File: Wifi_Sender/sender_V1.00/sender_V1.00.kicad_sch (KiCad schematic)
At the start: 2 parts, among them U1 ESP32-DevKitC, U2 L298N

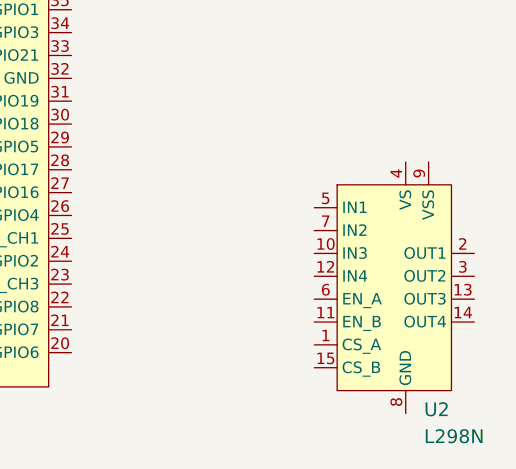
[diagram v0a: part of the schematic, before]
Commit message: Removed old Pics
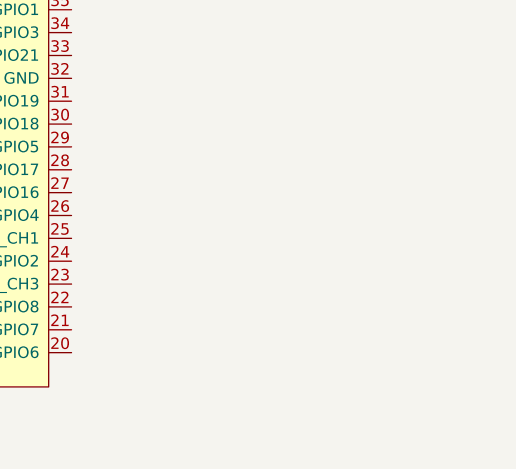
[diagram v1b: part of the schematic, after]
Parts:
- removed U2: L298N, digikey-footprints:Multiwatt-15, symbol dk_PMIC-Full-Half-Bridge-Drivers:L298N
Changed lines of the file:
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@@
-    (pin "9")
-  )
-  (symbol (lib_id "dk_PMIC-Full-Half-Bridge-Drivers:L298N") (at 142.748 55.0672 0) (unit 1)
-    (in_bom yes) (on_board yes) (fields_autoplaced)
-    (property "Reference" "U2" (id 0) (at 144.7674 72.4389 0)
-      (effects (font (size 1.524 1.524)) (justify left))
-    )
-    (property "Value" "L298N" (id 1) (at 144.7674 75.4323 0)
-      (effects (font (size 1.524 1.524)) (justify left))
-    )
-    (property "Footprint" "digikey-footprints:Multiwatt-15" (id 2) (at 147.828 49.9872 0)
-      (effects (font (size 1.524 1.524)) (justify left) hide)
-    )
-    (property "Datasheet" "http://www.st.com/content/ccc/resource/technical/document/datasheet/82/cc/3f/39/0a/29/4d/f0/CD00000240.pdf/files/CD00000240.pdf/jcr:content/translations/en.CD00000240.pdf" (id 3) (at 147.828 47.4472 0)
-      (effects (font (size 1.524 1.524)) (justify left) hide)
-    )
-    (property "Digi-Key_PN" "497-1395-5-ND" (id 4) (at 147.828 44.9072 0)
-      (effects (font (size 1.524 1.524)) (justify left) hide)
-    )
-    (property "MPN" "L298N" (id 5) (at 147.828 42.3672 0)
-      (effects (font (size 1.524 1.524)) (justify left) hide)
-    )
-    (property "Category" "Integrated Circuits (ICs)" (id 6) (at 147.828 39.8272 0)
-      (effects (font (size 1.524 1.524)) (justify left) hide)
-    )
-    (property "Family" "PMIC - Full, Half-Bridge Drivers" (id 7) (at 147.828 37.2872 0)
-      (effects (font (size 1.524 1.524)) (justify left) hide)
-    )
-    (property "DK_Datasheet_Link" "http://www.st.com/content/ccc/resource/technical/document/datasheet/82/cc/3f/39/0a/29/4d/f0/CD00000240.pdf/files/CD00000240.pdf/jcr:content/translations/en.CD00000240.pdf" (id 8) (at 147.828 34.7472 0)
-      (effects (font (size 1.524 1.524)) (justify left) hide)
-    )
-    (property "DK_Detail_Page" "/product-detail/en/stmicroelectronics/L298N/497-1395-5-ND/585918" (id 9) (at 147.828 32.2072 0)
-      (effects (font (size 1.524 1.524)) (justify left) hide)
-    )
-    (property "Description" "IC BRIDGE DRIVER PAR 15MULTIWATT" (id 10) (at 147.828 29.6672 0)
-      (effects (font (size 1.524 1.524)) (justify left) hide)
-    )
-    (property "Manufacturer" "STMicroelectronics" (id 11) (at 147.828 27.1272 0)
-      (effects (font (size 1.524 1.524)) (justify left) hide)
-    )
-    (property "Status" "Active" (id 12) (at 147.828 24.5872 0)
-      (effects (font (size 1.524 1.524)) (justify left) hide)
-    )
-    (pin "1")
-    (pin "10")
-    (pin "11")
-    (pin "12")
-    (pin "13")
-    (pin "14")
-    (pin "15")
-    (pin "2")
-    (pin "3")
-    (pin "4")
-    (pin "5")
-    (pin "6")
-    (pin "7")
-    (pin "8")
     (pin "9")
   )
@@
       (reference "U1") (unit 1) (value "ESP32-DevKitC") (footprint "Espressif:ESP32-DevKitC")
     )
-    (path "/bd775137-e24b-4a19-94a7-9ee7e74c8b52"
-      (reference "U2") (unit 1) (value "L298N") (footprint "digikey-footprints:Multiwatt-15")
-    )
   )

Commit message: Start Sender Design
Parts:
- removed U1: ESP32-DevKitC, Espressif:ESP32-DevKitC, symbol sender_V1.00-rescue:ESP32-DevKitC-Espressif
- added J?: Motor_2, symbol Connector:Screw_Terminal_01x03
- added J?: 9-12V Out, symbol Connector:Screw_Terminal_01x02
- added J?: Oled Screen, symbol Connector:Screw_Terminal_01x04
- added J?: Door_Open, symbol Connector:Screw_Terminal_01x02
- added J?: Door_Motor (5V), symbol Connector:Screw_Terminal_01x02
- added J?: I2C_1, symbol Connector:Screw_Terminal_01x04
- added J?: Light Sensor, symbol Connector:Screw_Terminal_01x03
- added J?: Motor_1, symbol Connector:Screw_Terminal_01x03
- added J?: 9-12V IN, symbol Connector:Screw_Terminal_01x02
- added J?: I2C_2, symbol Connector:Screw_Terminal_01x04
- added J?: Door_Closed, symbol Connector:Screw_Terminal_01x02
- added U?: ESP32-DEVKIT-V1, symbol teensy:ESP32-DEVKIT-V1
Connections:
- new net +3V3: J?.4 (Pin_4), J?.4 (Pin_4), J?.4 (Pin_4)
- new net GND: J?.3 (Pin_3), J?.3 (Pin_3), J?.3 (Pin_3)
- new net SCL: J?.2 (Pin_2), J?.2 (Pin_2), J?.2 (Pin_2)
- new net SDA: J?.1 (Pin_1), J?.1 (Pin_1), J?.1 (Pin_1)

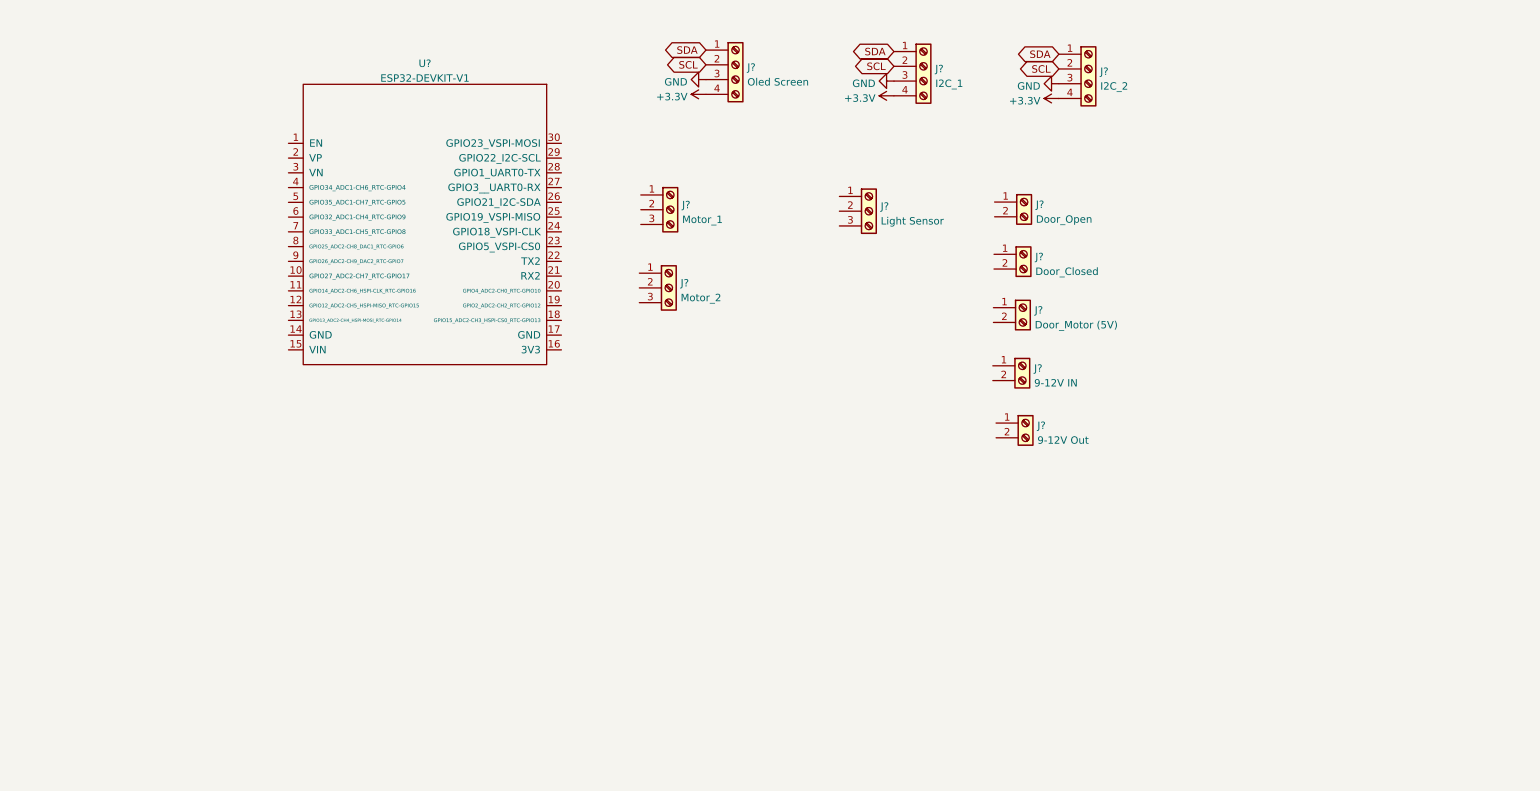
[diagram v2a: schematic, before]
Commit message: Start Design of Sender
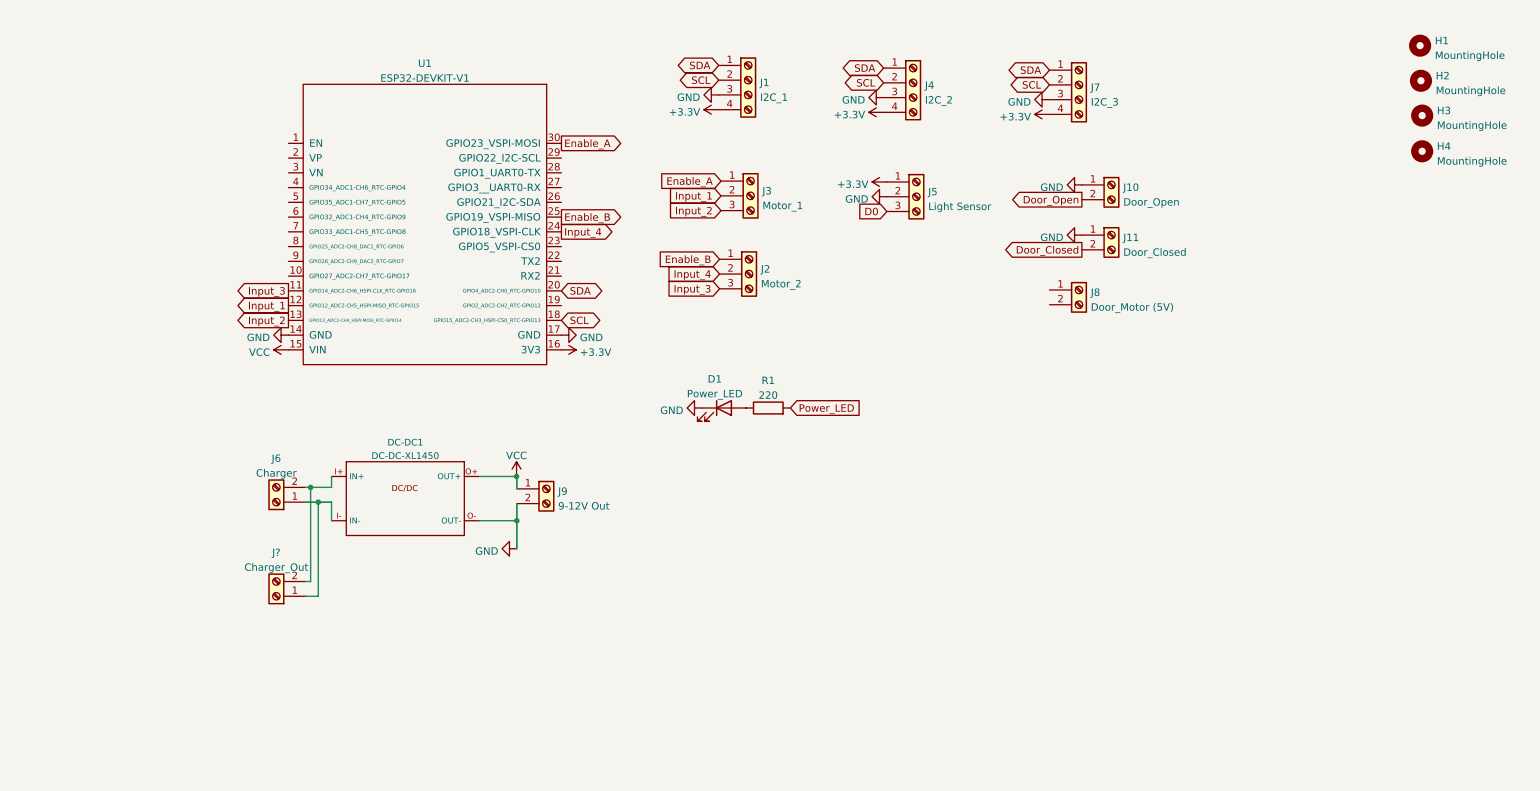
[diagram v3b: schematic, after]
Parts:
- added D1: Power_LED, LED_THT:LED_D5.0mm, symbol Device:LED
- added DC-DC1: DC-DC-XL1450, Zimprich:DCDC-XL1450, symbol Zimprich:DC-DC-XL1450
- added H1, H2, H3, H4: MountingHole, MountingHole:MountingHole_3.2mm_M3, symbol Mechanical:MountingHole
- added J?: Charger_Out, Connector_Phoenix_MSTB:PhoenixContact_MSTBVA_2,5_2-G-5,08_1x02_P5.08mm_Vertical, symbol Connector:Screw_Terminal_01x02
- added R1: 220, Resistor_THT:R_Axial_DIN0207_L6.3mm_D2.5mm_P10.16mm_Horizontal, symbol Device:R
- J1, J4: renamed from J?; footprint (none) -> Connector_JST:JST_XH_B4B-XH-A_1x04_P2.50mm_Vertical
- J10, J11, J8: renamed from J?; footprint (none) -> Connector_JST:JST_XH_B2B-XH-A_1x02_P2.50mm_Vertical
- J2, J3, J5: renamed from J?; footprint (none) -> Connector_JST:JST_XH_B3B-XH-A_1x03_P2.50mm_Vertical
- J6: renamed from J?; value 9-12V IN -> Charger; footprint (none) -> Connector_Phoenix_MSTB:PhoenixContact_MSTBVA_2,5_2-G-5,08_1x02_P5.08mm_Vertical
- J7: renamed from J?; value Oled Screen -> I2C_3; footprint (none) -> Connector_JST:JST_XH_B4B-XH-A_1x04_P2.50mm_Vertical
- J9: renamed from J?; footprint (none) -> Connector_Phoenix_MSTB:PhoenixContact_MSTBVA_2,5_2-G-5,08_1x02_P5.08mm_Vertical
- U1: renamed from U?; footprint (none) -> teensy_library-master:ESP32-DEVKIT-V1
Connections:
- net +3V3: now also J5.1 (Pin_1), U1.16 (3V3)
- net GND: now also J10.1 (Pin_1), J11.1 (Pin_1), J5.2 (Pin_2), J9.2 (Pin_2), U1.14 (GND), U1.17 (GND), D1.1 (K), DC-DC1.O- (OUT-)
- net SCL: now also U1.18 (GPIO15_ADC2-CH3_HSPI-CS0_RTC-GPIO13)
- net SDA: now also U1.20 (GPIO4_ADC2-CH0_RTC-GPIO10)
- net Enable_B: now reaches J2.1 (Pin_1)
- net Enable_B: now also U1.25 (GPIO19_VSPI-MISO)
- net Input_4: now reaches J2.2 (Pin_2)
- net Input_4: now also U1.24 (GPIO18_VSPI-CLK)
- net Input_3: now reaches J2.3 (Pin_3)
- net Input_3: now also U1.11 (GPIO14_ADC2-CH6_HSPI-CLK_RTC-GPIO16)
- net VCC: now reaches J9.1 (Pin_1)
- net VCC: now also U1.15 (VIN), DC-DC1.O+ (OUT+)
- net Door_Open: now reaches J10.2 (Pin_2)
- net D0: now reaches J5.3 (Pin_3)
- net Enable_A: now reaches J3.1 (Pin_1)
- net Enable_A: now also U1.30 (GPIO23_VSPI-MOSI)
- net Input_1: now reaches J3.2 (Pin_2)
- net Input_1: now also U1.12 (GPIO12_ADC2-CH5_HSPI-MISO_RTC-GPIO15)
- net Input_2: now reaches J3.3 (Pin_3)
- net Input_2: now also U1.13 (GPIO13_ADC2-CH4_HSPI-MOSI_RTC-GPIO14)
- net at J6.1 (Pin_1): now also DC-DC1.I- (IN-), J?.1 (Pin_1)
- net at J6.2 (Pin_2): now also DC-DC1.I+ (IN+), J?.2 (Pin_2)
- net Door_Closed: now reaches J11.2 (Pin_2)
- new net: D1.2 (A), R1.1
- new net Power_LED: R1.2
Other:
- moved on the sheet: J1, J10, J11, J2, J3, J4, J5, J6, J7, J8, J9

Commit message: Add Gerber Files
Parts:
- removed DC-DC1: DC-DC-XL1450, Zimprich:DCDC-XL1450, symbol Zimprich:DC-DC-XL1450
- removed J8: Door_Motor (5V), Connector_JST:JST_XH_B2B-XH-A_1x02_P2.50mm_Vertical, symbol Connector:Screw_Terminal_01x02
- removed J?: Charger_Out, Connector_Phoenix_MSTB:PhoenixContact_MSTBVA_2,5_2-G-5,08_1x02_P5.08mm_Vertical, symbol Connector:Screw_Terminal_01x02
- added SW1: PowerSwitch, Connector_PinHeader_2.54mm:PinHeader_1x02_P2.54mm_Vertical, symbol Switch:SW_Push
- J1: renamed from J6; value Charger -> 9-12V In
- renumbered J11 to J10, J9 to J2, J1 to J3, J2 to J4, J3 to J5, J4 to J6, J5 to J7, J7 to J8, J10 to J9
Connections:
- net Power_LED is gone; now on net +3V3: R1.2
- net D0: now also U1.5 (GPIO35_ADC1-CH7_RTC-GPIO5)
- net GND: now also J1.2 (Pin_2)
- net at J1.1 (Pin_1): now also SW1.1
- net VCC: no longer names the net of J2.1 (Pin_1), U1.15 (VIN)
- net VCC: now also SW1.2
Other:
- moved on the sheet: D1, J1, J2, R1

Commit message: Update
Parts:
- removed D1: Power_LED, LED_THT:LED_D5.0mm, symbol Device:LED
- added DC-DC1: DC-DC-XL1450, Zimprich:DCDC-XL1450, symbol Zimprich:DC-DC-XL1450
- added J12: 5V IN, Connector_JST:JST_XH_B2B-XH-A_1x02_P2.50mm_Vertical, symbol Connector:Screw_Terminal_01x02
- added J2: Charge Out, Connector_Phoenix_MSTB:PhoenixContact_MSTBVA_2,5_2-G-5,08_1x02_P5.08mm_Vertical, symbol Connector:Screw_Terminal_01x02
- added J9: Green_Red_Led, Connector_JST:JST_XH_B3B-XH-A_1x03_P2.50mm_Vertical, symbol Connector:Screw_Terminal_01x03
- added R2: 220, Resistor_THT:R_Axial_DIN0207_L6.3mm_D2.5mm_P10.16mm_Horizontal, symbol Device:R
- added U1, U3: INA226-Sense_I2C, Current_sense:INA226, symbol charge_pcb-rescue:INA226-Sense_I2C
- J1: value 9-12V In -> Charger
- R1: value 220 -> 2K2
- renumbered J9 to J10, J10 to J11, J8 to J13, J2 to J3, J3 to J4, J4 to J5, J5 to J6, J6 to J7, J7 to J8, U1 to U2
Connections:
- net +3V3: now also U1.8 (VCC), U3.8 (VCC); no longer R1.2, U2.16 (3V3)
- net D0: now also U2.6 (GPIO32_ADC1-CH4_RTC-GPIO9); no longer U2.5 (GPIO35_ADC1-CH7_RTC-GPIO5)
- net Door_Closed: now also U2.5 (GPIO35_ADC1-CH7_RTC-GPIO5)
- net Door_Open: now also U2.4 (GPIO34_ADC1-CH6_RTC-GPIO4)
- net GND: now also DC-DC1.I- (IN-), DC-DC1.O- (OUT-), J12.1 (Pin_1), J2.2 (Pin_2), J9.1 (Pin_1), U1.7 (GND), U3.7 (GND)
- net SCL: now also U2.29 (GPIO22_I2C-SCL), U1.5 (SCL), U3.5 (SCL); no longer U2.18 (GPIO15_ADC2-CH3_HSPI-CS0_RTC-GPIO13)
- net SDA: now also U2.26 (GPIO21_I2C-SDA), U1.6 (SDA), U3.6 (SDA); no longer U2.20 (GPIO4_ADC2-CH0_RTC-GPIO10)
- net at R1.1: now also J9.2 (Pin_2)
- net Green: now reaches U2.8 (GPIO25_ADC2-CH8_DAC1_RTC-GPIO6)
- net Green: now also R2.2
- net RED: now reaches U2.9 (GPIO26_ADC2-CH9_DAC2_RTC-GPIO7)
- net RED: now also R1.2
- new net: J3.1 (Pin_1), U3.10 (IN1-)
- new net: DC-DC1.O+ (OUT+), U3.3 (VBS), U3.9 (IN1+)
- new net: J9.3 (Pin_3), R2.1
- new net: J2.1 (Pin_1), U1.10 (IN1-)
- new net: DC-DC1.I+ (IN+), SW1.2, U1.3 (VBS), U1.9 (IN1+)
- new net: J12.2 (Pin_2), U2.15 (VIN)
- no-connect marks 0 -> 19
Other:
- title: (none) -> Wifi Perimeter Sender
- moved on the sheet: J10, J11, J3, U2

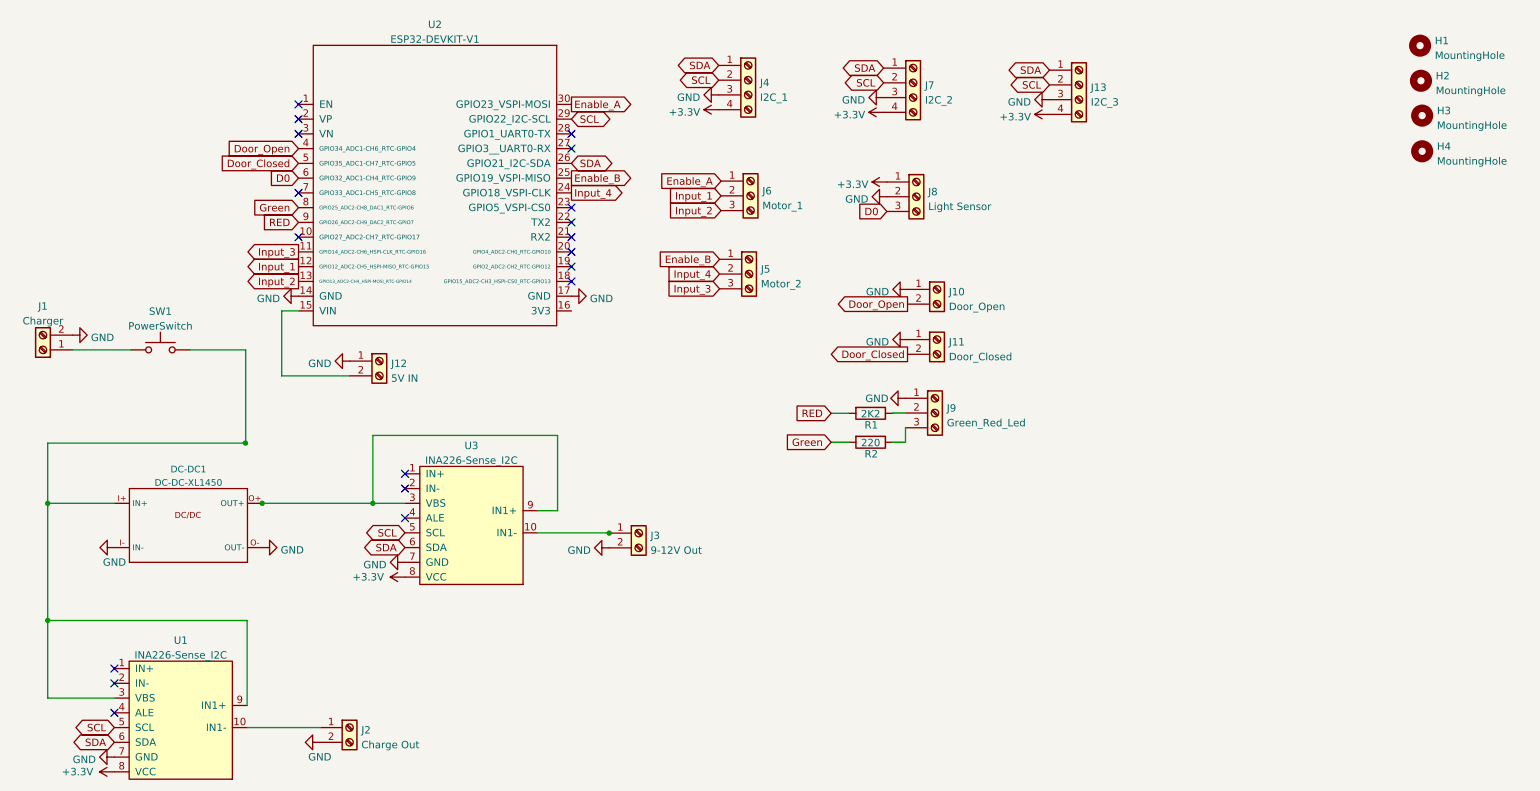
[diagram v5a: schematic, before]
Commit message: Add Tracks
Tracks added
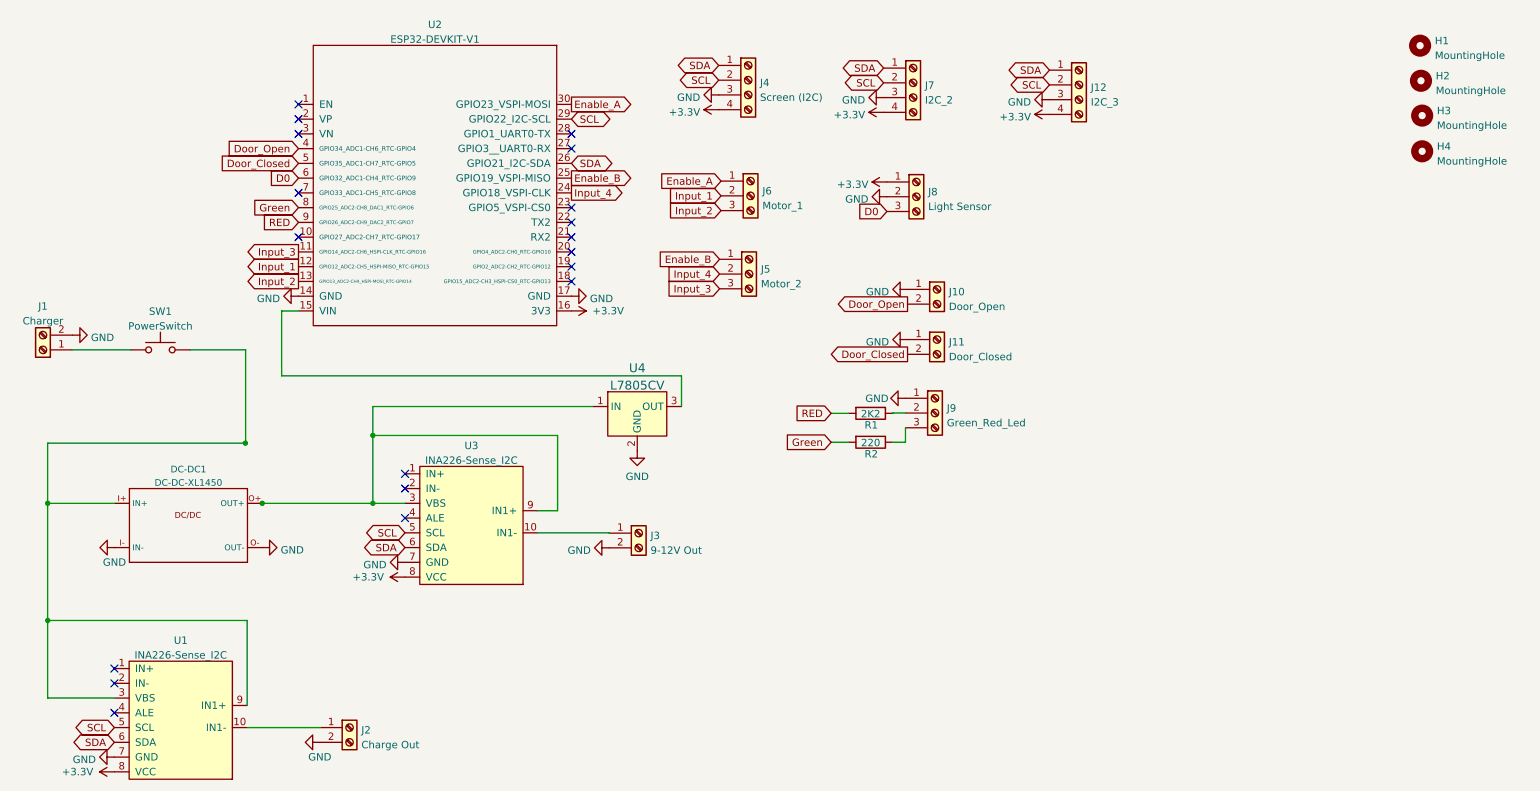
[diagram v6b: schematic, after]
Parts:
- removed J12: 5V IN, Connector_JST:JST_XH_B2B-XH-A_1x02_P2.50mm_Vertical, symbol Connector:Screw_Terminal_01x02
- added U4: L7805CV, digikey-footprints:TO-220-3, symbol dk_PMIC-Voltage-Regulators-Linear:L7805CV
- J4: value I2C_1 -> Screen (I2C)
- renumbered J13 to J12
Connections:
- net +3V3: now also U2.16 (3V3)
- net GND: now also U4.2 (GND)
- net at DC-DC1.O+ (OUT+), U3.3 (VBS), U3.9 (IN1+): now also U4.1 (IN)
- net at U2.15 (VIN): now also U4.3 (OUT)
